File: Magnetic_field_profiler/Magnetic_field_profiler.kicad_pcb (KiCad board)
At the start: 4 copper layers, 130 x 100 mm, 119 parts, among them J1 USB_B_Micro, J2 Screw_Terminal_01x02, J3 Conn_01x04_Socket, J4 Conn_01x04_Socket, Q1 BSS123, SW1 SW_SPDT, U1 STM32F103C8Tx, U10 MLX90393, U11 MLX90393, U12 MLX90393, U13 MLX90393, U14 MLX90393, U15 MLX90393, U16 MLX90393, U17 MLX90393, U18 MLX90393, U19 MLX90393, U2 AP63203WU, U20 MLX90393, U21 MLX90393, U3 MCP23S17, U4 DRV8825, U5 DRV8825, U6 MLX90393, U7 MLX90393, U8 MLX90393, U9 MLX90393, Y1 Crystal_GND24

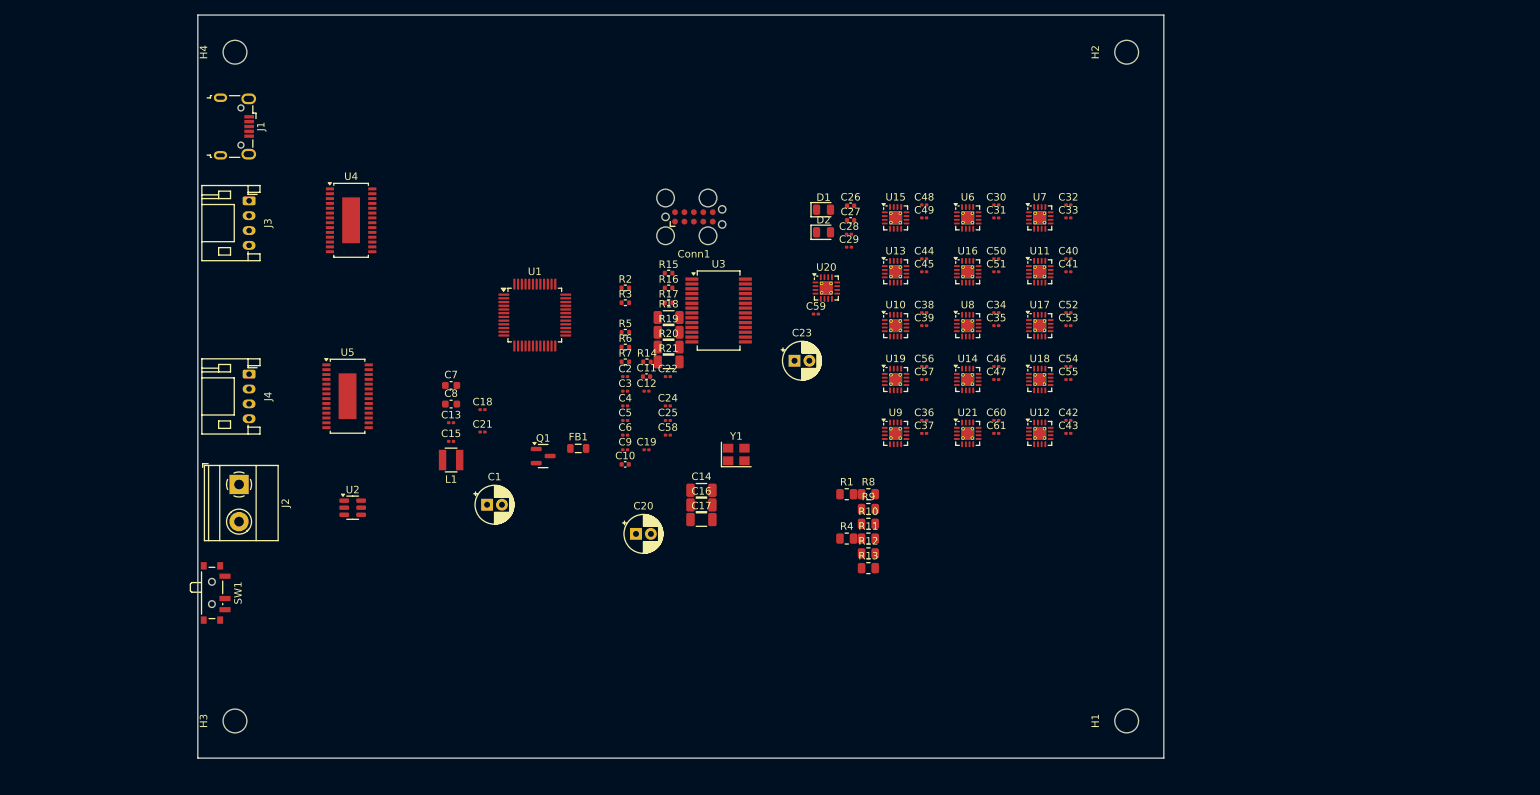
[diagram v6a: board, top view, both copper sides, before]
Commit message: Initial component placement
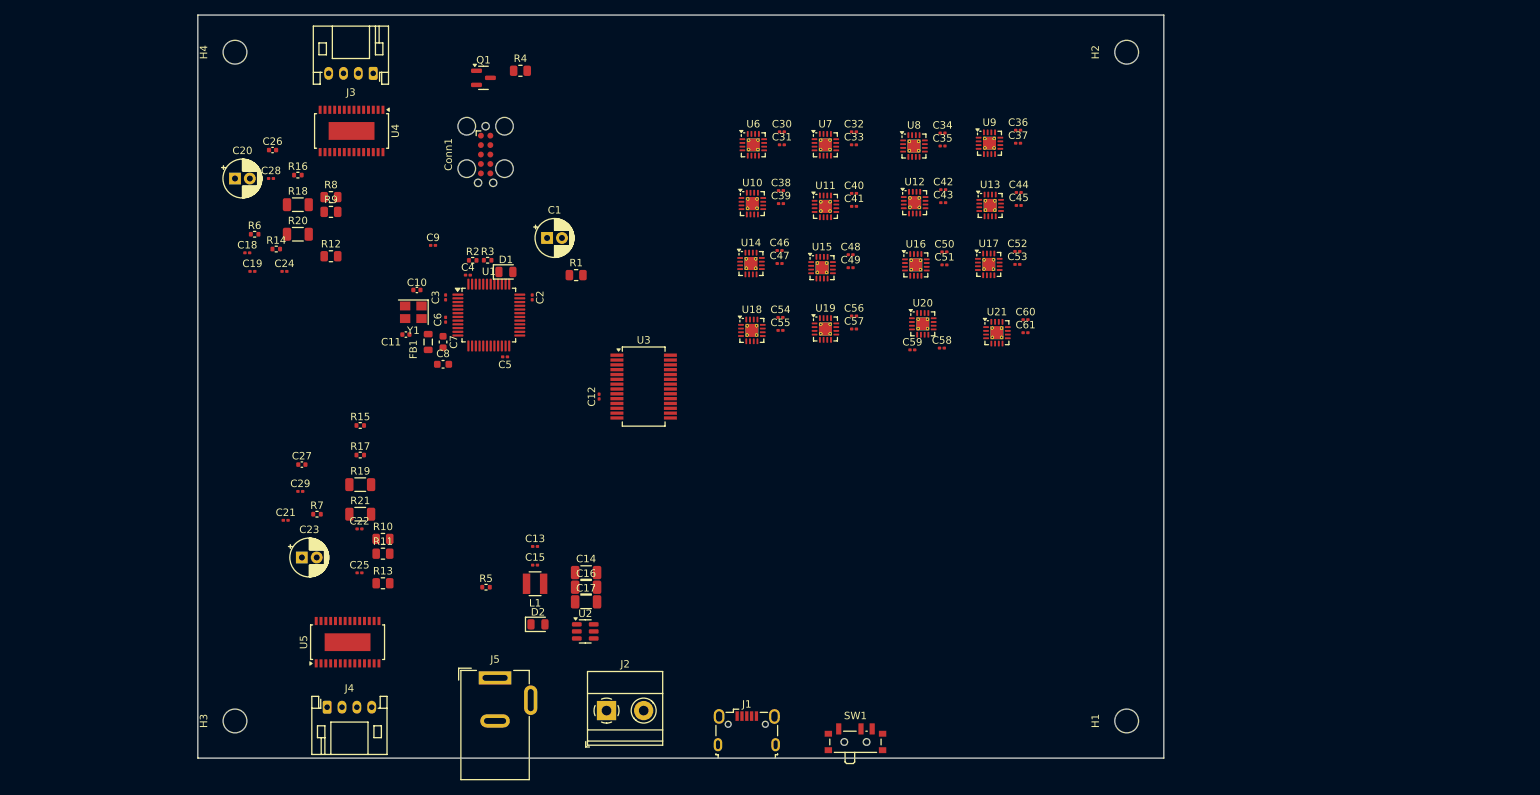
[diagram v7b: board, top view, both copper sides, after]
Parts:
- added J5: Barrel_Jack, Connector_BarrelJack:BarrelJack_Wuerth_6941xx301002, F.Cu at (90.0, 139.2)
- Y1: value Crystal_GND24 -> 16MHz
- moved J1 106.5 mm to (123.9, 146.2), turned to 0 degrees
- moved SW1 88.5 mm to (138.5, 147.5), turned to 0 degrees
- moved R12 82.6 mm to (67.9, 82.5)
- moved R8 82.6 mm to (67.9, 74.5)
- moved R9 82.6 mm to (67.9, 76.5)
- moved C27 80.8 mm to (64.0, 110.5)
- moved C29 80.8 mm to (63.8, 114.1)
- moved C26 78.1 mm to (60.1, 68.2)
- moved C28 78.1 mm to (59.8, 72.0)
- moved R4 76.8 mm to (93.4, 57.5)
- moved C20 72.1 mm to (55.0, 72.0)
- moved C23 71.4 mm to (64.0, 123.0)
- moved R10 65.4 mm to (74.9, 120.5)
- moved R11 65.4 mm to (74.9, 122.5)
- moved R13 65.4 mm to (74.9, 126.5)
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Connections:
- net /IO_CS renamed /IO1_CS
- net /IO_RST renamed /IO1_RST
- net Net-(D1-A) renamed /STATUS_LED
- net Net-(D1-K) renamed /R_LED
- J1 pad 1: +5V -> unconnected-(J1-VBUS-Pad1)
- U1 pad 29: unconnected-(U1-PA8-Pad29) -> /MTR_DECAY
- U4 pad 19: unconnected-(U4-DECAY-Pad19) -> /MTR_DECAY
- U5 pad 19: unconnected-(U5-DECAY-Pad19) -> /MTR_DECAY
